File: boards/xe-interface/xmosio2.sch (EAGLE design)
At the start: 109 parts, among them IC1 IDTQS3245QSOP20, IC2 IDTQS3245QSOP20, IC3 IDTQS3245QSOP20, IC4 IDTQS3245QSOP20, IC5 IDTQS3245QSOP20, U1 24 MHz Osc. (F535L-24), U2 USD-SOCKETNEW, X1 0446200002

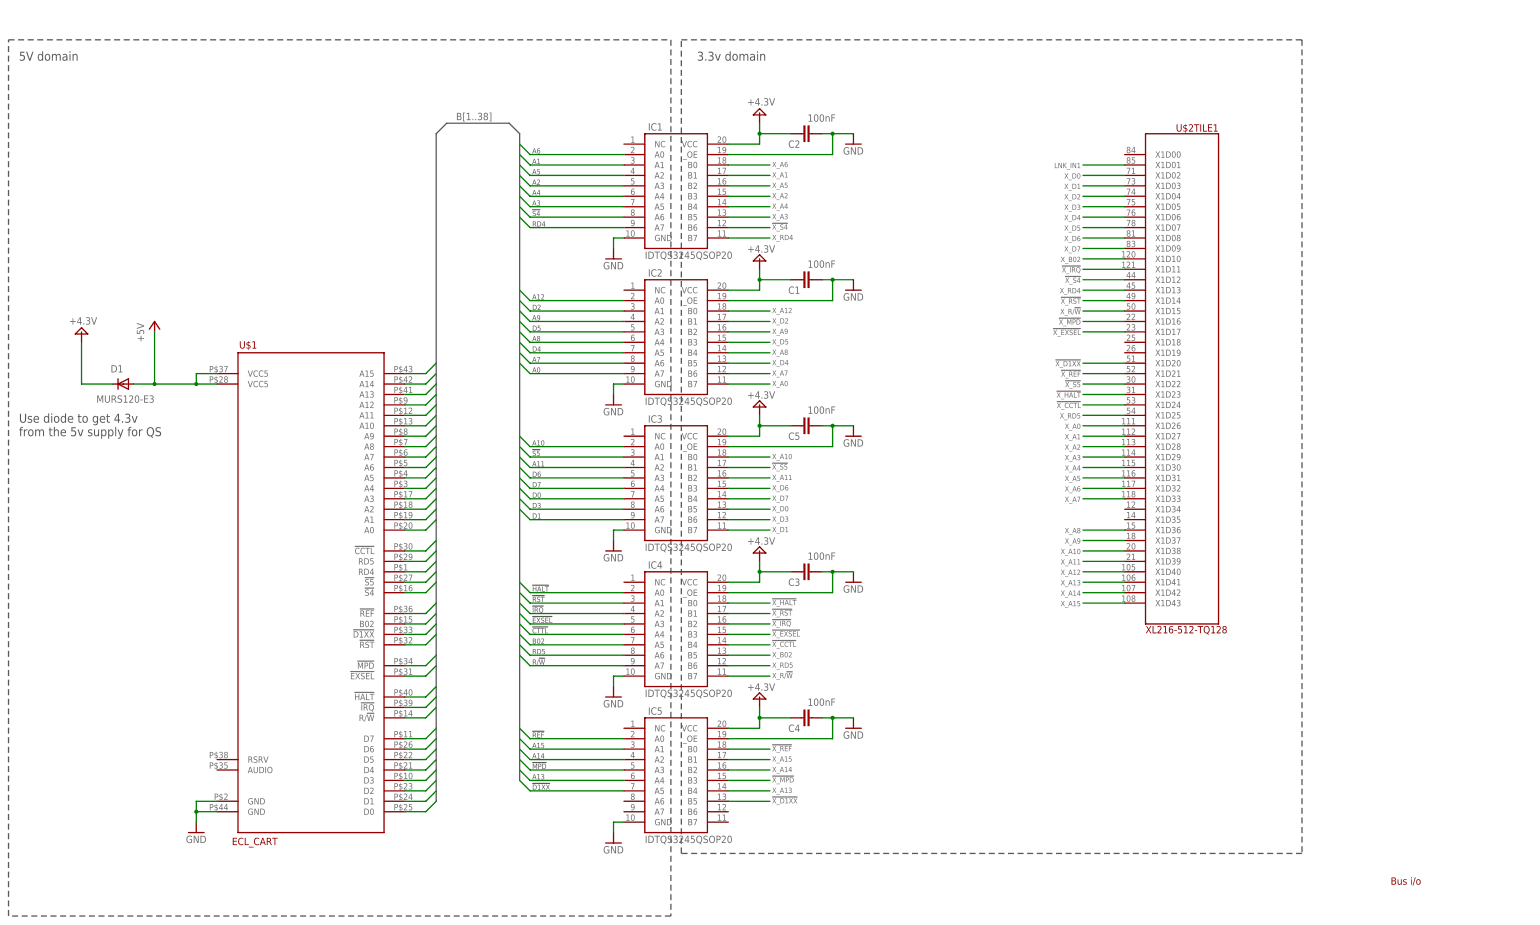
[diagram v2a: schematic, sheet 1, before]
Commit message: Latest fixes and additions  - screw holes  - cartridge slot  - PBI device selection DIP switch  - Memory interface style DIP switch
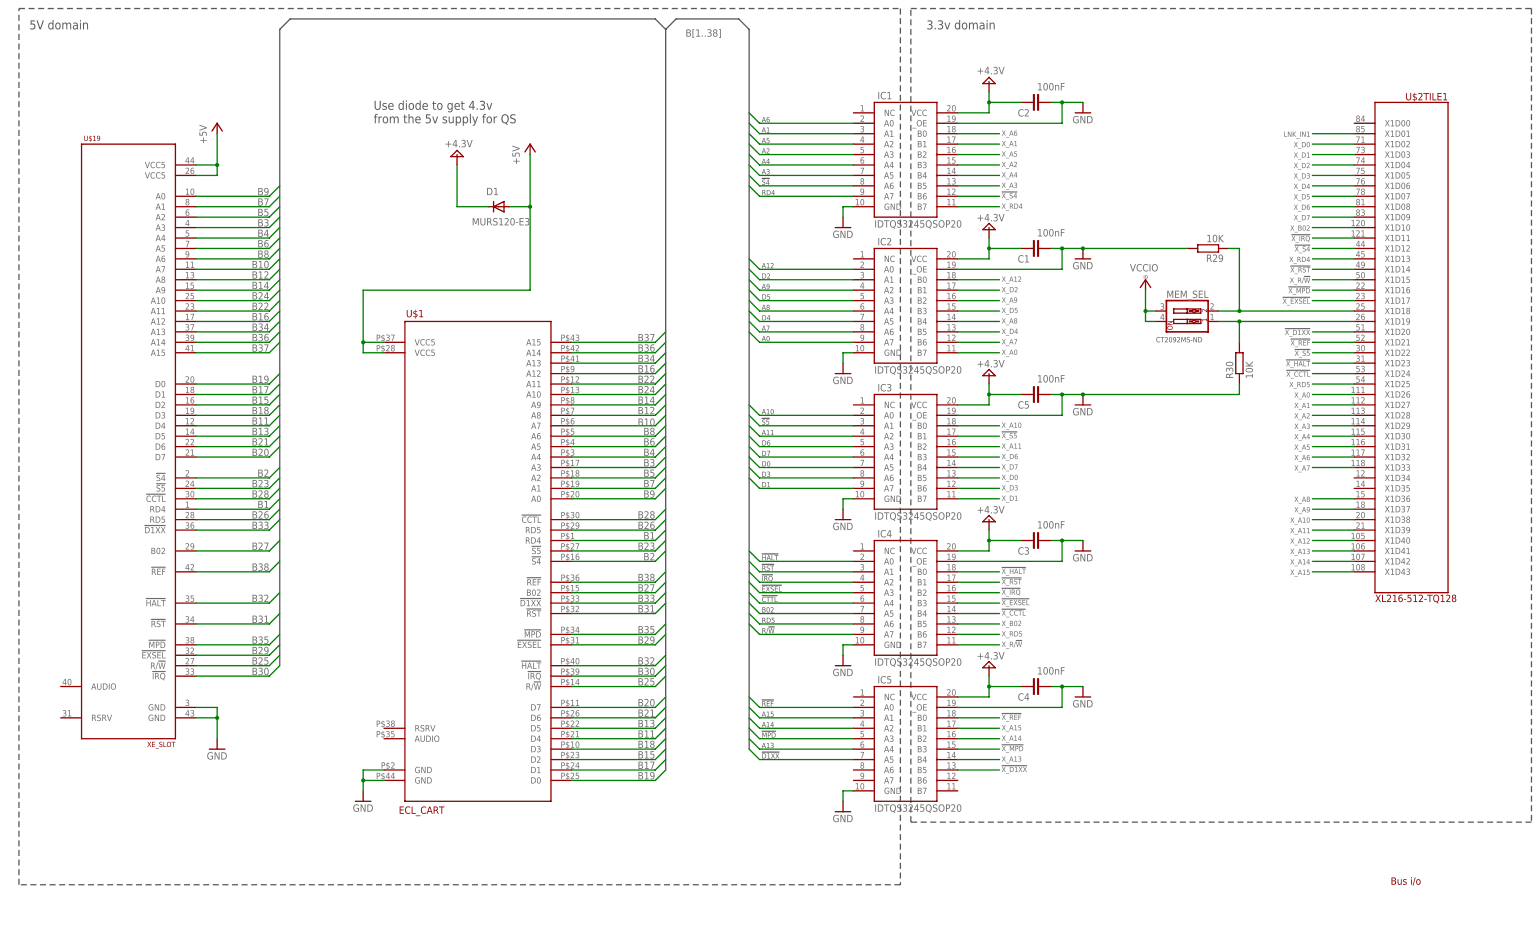
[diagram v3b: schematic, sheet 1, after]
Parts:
- added H1, H2, H3, H4: MOUNT-HOLE3.2, holes:MOUNT-HOLE3.2
- added MEM_SEL: (no value), special:SW_DIP-2
- added PBI_ID: (no value), special:SW_DIP-3
- added R29, R30, R31, R33, R34: 10K, rcl:R-EU_R1206
- added U$19: XE_SLOT, pbxl:XE_SLOT
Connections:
- new net N$34: MEM_SEL.2, R29.1, U$2TILE1.X1D18@25
- new net N$35: MEM_SEL.1, R30.2, U$2TILE1.X1D19@26
- new net PBI0: PBI_ID.1, R31.2, U$2TILE0.X0D11@33
- new net PBI1: PBI_ID.2, R34.2, U$2TILE0.X0D12@61
- new net PBI2: PBI_ID.3, R33.2, U$2TILE0.X0D13@62
- net +5V: now also U$19.VCC5@13, U$19.VCC5@7
- net B1: now also U$19.RD4@A
- net B10: now also U$19.A7@F
- net B11: now also U$19.D4@6
- net B12: now also U$19.A8@H
- net B13: now also U$19.D5@7
- net B14: now also U$19.A9@J
- net B15: now also U$19.D2@8
- net B16: now also U$19.A12@K
- net B17: now also U$19.D1@9
- net B18: now also U$19.D3@L
- net B19: now also U$19.D0@10
- net B2: now also U$19.!S4!@1
- net B20: now also U$19.D7@M
- net B21: now also U$19.D6@11
- net B22: now also U$19.A11@N
- net B23: now also U$19.!S5!@12
- net B24: now also U$19.A10@P
- net B25: now also U$19.R/!W!@R
- net B26: now also U$19.RD5@14
- net B27: now also U$19.B02@S
- net B28: now also U$19.!CCTL!@15
- net B29: now also U$19.!EXSEL!@1
- net B3: now also U$19.A3@2
- net B30: now also U$19.!IRQ!@B
- net B31: now also U$19.!RST!@2
- net B32: now also U$19.!HALT!@C
- net B33: now also U$19.!D1XX!@3
- net B34: now also U$19.A13@D
- net B35: now also U$19.!MPD!@4
- net B36: now also U$19.A14@E
- net B37: now also U$19.A15@F
- net B38: now also U$19.!REF!@6
- net B4: now also U$19.A4@C
- net B5: now also U$19.A2@3
- net B6: now also U$19.A5@D
- net B7: now also U$19.A1@4
- net B8: now also U$19.A6@E
- net B9: now also U$19.A0@5
- net GND: now also R29.2, R30.1, R31.1, R33.1, R34.1, U$19.GND@B, U$19.GND@H
- net VCCIO: now also MEM_SEL.3, MEM_SEL.4, PBI_ID.4, PBI_ID.5, PBI_ID.6
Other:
- note added: "CT2092MS-ND"
- note added: "CT2093MS-ND"
- moved on the sheet: C1, C2, C3, C35, C36, C37, C38, C39, C4, C40, C41, C5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

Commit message: Latest board (routed and unrolled)
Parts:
- added GPIO: (no value), pinhead:PINHD-1X4
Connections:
- new net N$36: GPIO.3, U$2TILE1.X1D34@12
- new net N$37: GPIO.2, U$2TILE1.X1D35@14
- net GND: now also GPIO.1
- net VCCIO: now also GPIO.4
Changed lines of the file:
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@@
 <setting verticaltext="up"/>
 </settings>
-<grid distance="0.1" unitdist="inch" unit="inch" style="lines" multiple="1" display="yes" altdistance="0.01" altunitdist="inch" altunit="inch"/>
+<grid distance="0.1" unitdist="inch" unit="inch" style="lines" multiple="1" display="no" altdistance="0.01" altunitdist="inch" altunit="inch"/>
 <layers>
 <layer number="1" name="Top" color="4" fill="1" visible="no" active="no"/>
@@
 <part name="GND49" library="supply1" deviceset="GND" device=""/>
 <part name="P+5" library="supply1" deviceset="+5V" device=""/>
+<part name="GPIO" library="pinhead" deviceset="PINHD-1X4" device=""/>
+<part name="GND50" library="supply1" deviceset="GND" device=""/>
+<part name="VCC29" library="supply1" deviceset="VCCIO" device=""/>
 </parts>
 <sheets>
@@
 <instance part="GND49" gate="1" x="-2.54" y="22.86"/>
 <instance part="P+5" gate="1" x="-2.54" y="175.26"/>
+<instance part="GPIO" gate="A" x="238.76" y="88.9" rot="R180"/>
+<instance part="GND50" gate="1" x="248.92" y="76.2"/>
+<instance part="VCC29" gate="G$1" x="248.92" y="99.06" smashed="yes">
+<attribute name="VALUE" x="245.11" y="101.092" size="1.778" layer="96"/>
+</instance>
 </instances>
 <busses>
@@
 <wire x1="-2.54" y1="33.02" x2="-2.54" y2="30.48" width="0.1524" layer="91"/>
 <junction x="-2.54" y="30.48"/>
+</segment>
+<segment>
+<pinref part="GND50" gate="1" pin="GND"/>
+<pinref part="GPIO" gate="A" pin="1"/>
+<wire x1="248.92" y1="78.74" x2="248.92" y2="83.82" width="0.1524" layer="91"/>
+<wire x1="248.92" y1="83.82" x2="241.3" y2="83.82" width="0.1524" layer="91"/>
 </segment>
 </net>
@@
 <junction x="223.52" y="129.54"/>
 </segment>
-</net>
+<segment>
+<pinref part="GPIO" gate="A" pin="4"/>
+<pinref part="VCC29" gate="G$1" pin="VCCIO"/>
+<wire x1="241.3" y1="91.44" x2="248.92" y2="91.44" width="0.1524" layer="91"/>
+<wire x1="248.92" y1="91.44" x2="248.92" y2="96.52" width="0.1524" layer="91"/>
+</segment>
+</net>
+<net name="N$36" class="0">
+<segment>
+<pinref part="U$2" gate="TILE1" pin="X1D34@12"/>
+<pinref part="GPIO" gate="A" pin="3"/>
+<wire x1="274.32" y1="88.9" x2="241.3" y2="88.9" width="0.1524" layer="91"/>
+</segment>
+</net>
+<net name="N$37" class="0">
+<segment>
+<pinref part="U$2" gate="TILE1" pin="X1D35@14"/>
+<pinref part="GPIO" gate="A" pin="2"/>
+<wire x1="274.32" y1="86.36" x2="241.3" y2="86.36" width="0.1524" layer="91"/>
+</segment>
+</net>

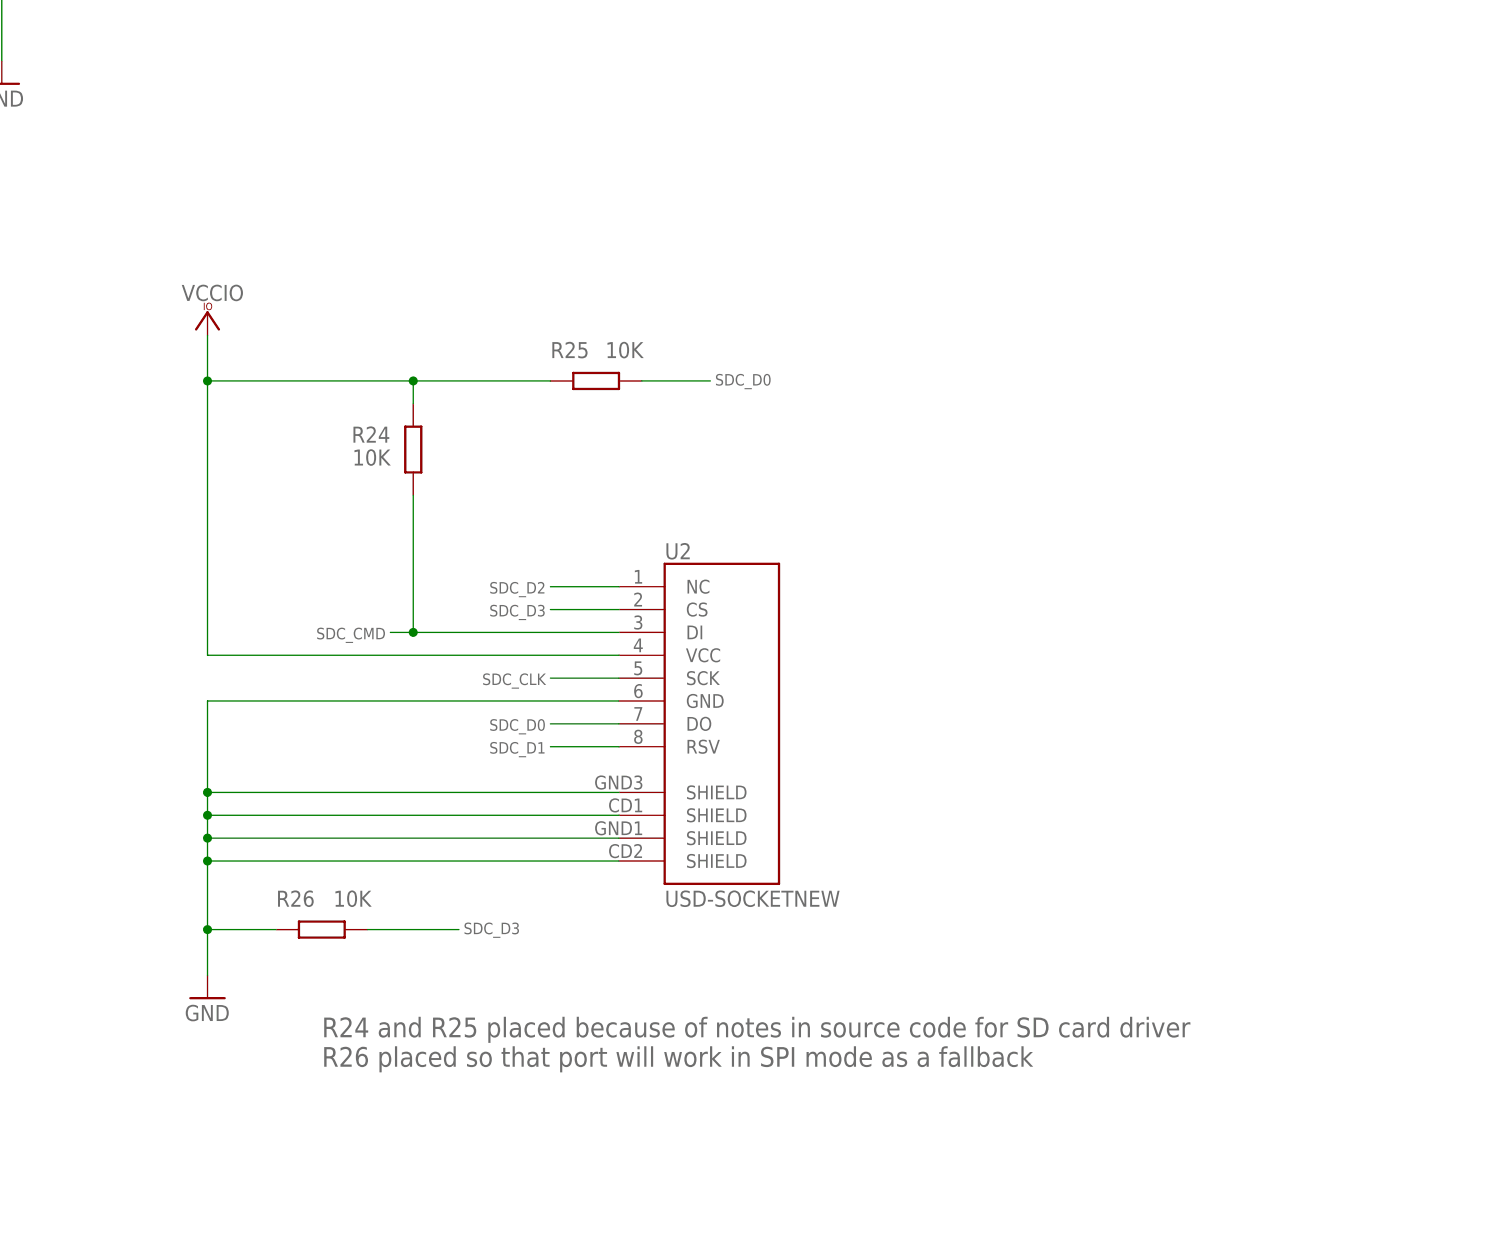
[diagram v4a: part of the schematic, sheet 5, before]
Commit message: Latest design changes  - Move the XTAG connector back significantly, so the shroud is not overhanging the board  - Use the SD card slot, not the micro-SD card, it’s easier to solder  - Fix the SD card pinouts  - Remove an unwanted pull-up on the SD card
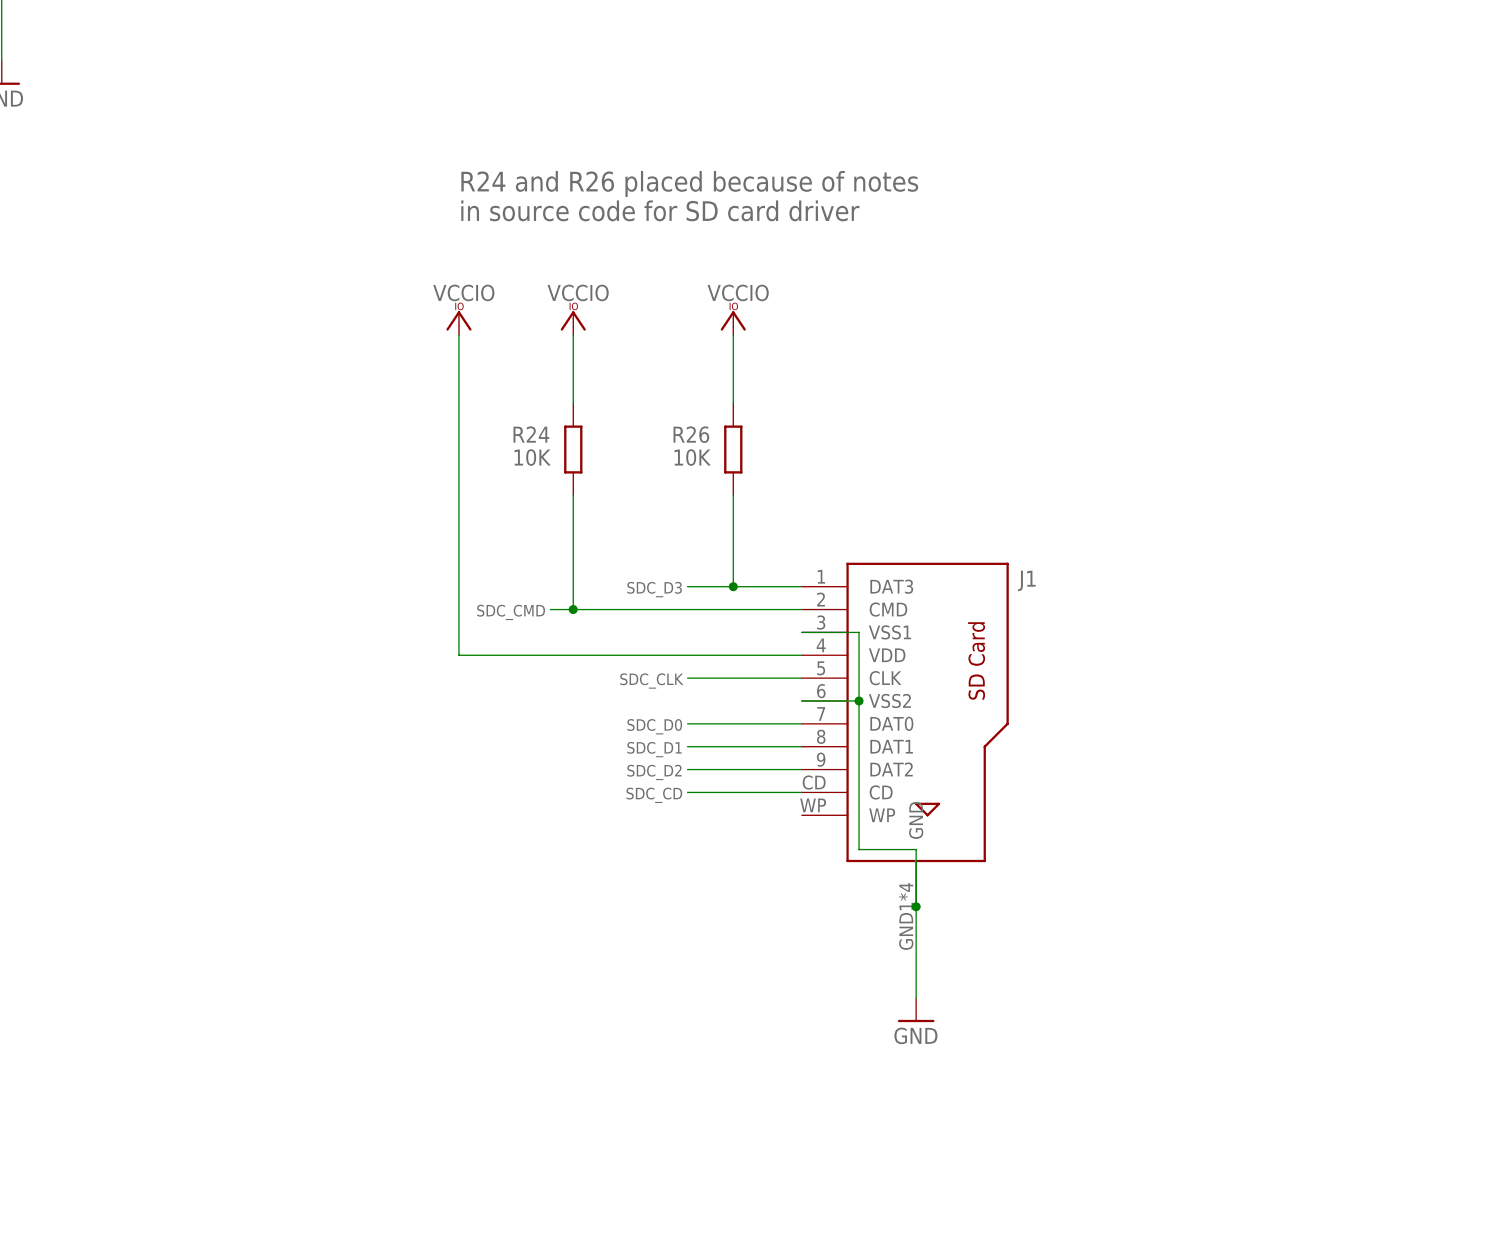
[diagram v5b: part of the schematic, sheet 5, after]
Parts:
- removed R25: 10K, rcl:R-EU_R1206
- removed U2: USD-SOCKETNEW, SparkFun-Connectors:USD-SOCKETNEW
- added J1: (no value), InputOutputIO (rev17e):693063020911
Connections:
- new net SDC_CD: U$2TILE1.X1D00@84
- net GND: now also J1.GND, J1.VSS1, J1.VSS2; no longer R26.2, U2.GND, U2.SHIELD@1, U2.SHIELD@2, U2.SHIELD@3, U2.SHIELD@4
- net SDC_CLK: now also U$2TILE0.X0D23@64; no longer U$2TILE0.X0D33@96, U2.SCK
- net SDC_CMD: now also U$2TILE0.X0D22@63; no longer U$2TILE0.X0D32@94, U2.DI
- net SDC_D0: now also U$2TILE0.X0D33@96; no longer R25.1, U$2TILE0.X0D27@93, U2.DO
- net SDC_D1: now also U$2TILE0.X0D32@94; no longer U$2TILE0.X0D26@92, U2.RSV
- net SDC_D2: now also U$2TILE0.X0D27@93; no longer U$2TILE0.X0D23@64, U2.NC
- net SDC_D3: now also R26.2, U$2TILE0.X0D26@92; no longer R26.1, U$2TILE0.X0D22@63, U2.CS
- net VCCIO: now also R26.1; no longer R25.2, U2.VCC
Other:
- note added: "R24 and R26 placed because of notes in source code for SD card driver"
- note removed: "R24 and R25 placed because of notes in source code for SD card driver R26 placed so that port will work in SPI mode as a fallback"
- moved on the sheet: R24, R26
